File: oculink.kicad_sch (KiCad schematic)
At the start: 17 parts, among them J4 OCuLink_x4_Amphenol_G14A42121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, U10 ESD204DQAR, U11 ESD204DQAR, U8 ESD204DQAR, U9 ESD204DQAR

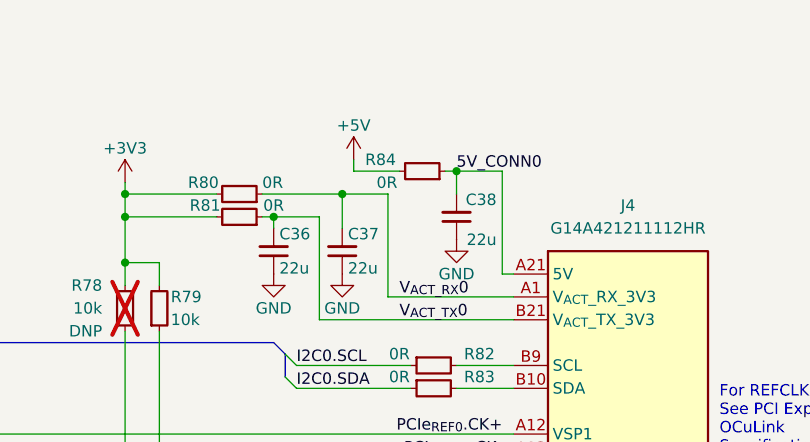
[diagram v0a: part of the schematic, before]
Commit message: [#58137] Add DC/DC supplies
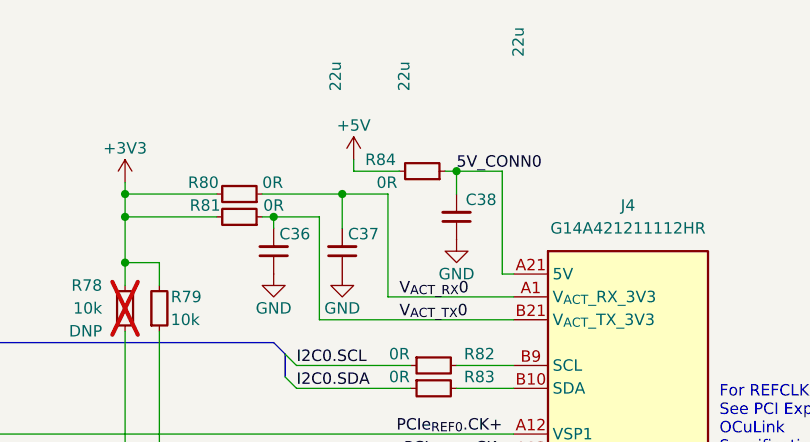
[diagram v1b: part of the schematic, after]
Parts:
- C36, C37, C38: value C_22u_0603 -> C_22u_16V_0603; symbol antmicroCapacitors0603:C_22u_0603 -> antmicroCapacitors0603:C_22u_16V_0603; MPN GRM188R60J226MEA0D -> CL10A226MO7JZNC; Manufacturer Murata -> Samsung Electro-Mechanics; Voltage (none) -> 16V
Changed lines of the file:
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@@
     (effects (font (size 1.27 1.27)) (justify right))
   )
-  (symbol (lib_id "antmicroCapacitors0603:C_22u_0603") (at 231.14 95.25 90) (unit 1)
+  (symbol (lib_id "antmicroCapacitors0603:C_22u_16V_0603") (at 231.14 95.25 90) (unit 1)
     (in_bom yes) (on_board yes) (dnp no)
     (property "Reference" "C38" (at 235.585 90.805 90)
       (effects (font (size 1.27 1.27) (thickness 0.15)) (justify left))
     )
-    (property "Value" "C_22u_0603" (at 241.3 74.93 0)
+    (property "Value" "C_22u_16V_0603" (at 241.3 74.93 0)
       (effects (font (size 1.27 1.27) (thickness 0.15)) (justify left bottom) hide)
     )
@@
       (effects (font (size 1.27 1.27) (thickness 0.15)) (justify left bottom) hide)
     )
-    (property "Datasheet" "https://www.murata.com/products/productdetail?partno=GRM188R60J226MEA0%23" (at 246.38 74.93 0)
-      (effects (font (size 1.27 1.27) (thickness 0.15)) (justify left bottom) hide)
-    )
-    (property "MPN" "GRM188R60J226MEA0D" (at 248.92 74.93 0)
-      (effects (font (size 1.27 1.27) (thickness 0.15)) (justify left bottom) hide)
-    )
-    (property "Manufacturer" "Murata" (at 251.46 74.93 0)
+    (property "Datasheet" "https://product.samsungsem.com/mlcc/CL10A226MO7JZN.do" (at 246.38 74.93 0)
+      (effects (font (size 1.27 1.27) (thickness 0.15)) (justify left bottom) hide)
+    )
+    (property "MPN" "CL10A226MO7JZNC" (at 248.92 74.93 0)
+      (effects (font (size 1.27 1.27) (thickness 0.15)) (justify left bottom) hide)
+    )
+    (property "Manufacturer" "Samsung Electro-Mechanics" (at 251.46 74.93 0)
       (effects (font (size 1.27 1.27) (thickness 0.15)) (justify left bottom) hide)
     )
@@
       (effects (font (size 1.27 1.27) (thickness 0.15)) (justify left bottom) hide)
     )
-    (property "Val" "22u" (at 235.585 95.25 90)
-      (effects (font (size 1.27 1.27) (thickness 0.15)) (justify left))
-    )
-    (property "Voltage" "" (at 259.08 74.93 0)
+    (property "Val" "22u" (at 238.76 74.93 0)
+      (effects (font (size 1.27 1.27) (thickness 0.15)) (justify left bottom))
+    )
+    (property "Voltage" "16V" (at 259.08 74.93 0)
       (effects (font (size 1.27 1.27)) (justify left bottom) hide)
     )
@@
     )
   )
-  (symbol (lib_id "antmicroCapacitors0603:C_22u_0603") (at 210.82 99.06 90) (unit 1)
+  (symbol (lib_id "antmicroCapacitors0603:C_22u_16V_0603") (at 210.82 99.06 90) (unit 1)
     (in_bom yes) (on_board yes) (dnp no)
     (property "Reference" "C36" (at 211.455 94.615 90)
       (effects (font (size 1.27 1.27) (thickness 0.15)) (justify right))
     )
-    (property "Value" "C_22u_0603" (at 220.98 78.74 0)
+    (property "Value" "C_22u_16V_0603" (at 220.98 78.74 0)
       (effects (font (size 1.27 1.27) (thickness 0.15)) (justify left bottom) hide)
     )
@@
       (effects (font (size 1.27 1.27) (thickness 0.15)) (justify left bottom) hide)
     )
-    (property "Datasheet" "https://www.murata.com/products/productdetail?partno=GRM188R60J226MEA0%23" (at 226.06 78.74 0)
-      (effects (font (size 1.27 1.27) (thickness 0.15)) (justify left bottom) hide)
-    )
-    (property "MPN" "GRM188R60J226MEA0D" (at 228.6 78.74 0)
-      (effects (font (size 1.27 1.27) (thickness 0.15)) (justify left bottom) hide)
-    )
-    (property "Manufacturer" "Murata" (at 231.14 78.74 0)
+    (property "Datasheet" "https://product.samsungsem.com/mlcc/CL10A226MO7JZN.do" (at 226.06 78.74 0)
+      (effects (font (size 1.27 1.27) (thickness 0.15)) (justify left bottom) hide)
+    )
+    (property "MPN" "CL10A226MO7JZNC" (at 228.6 78.74 0)
+      (effects (font (size 1.27 1.27) (thickness 0.15)) (justify left bottom) hide)
+    )
+    (property "Manufacturer" "Samsung Electro-Mechanics" (at 231.14 78.74 0)
       (effects (font (size 1.27 1.27) (thickness 0.15)) (justify left bottom) hide)
     )
@@
       (effects (font (size 1.27 1.27) (thickness 0.15)) (justify left bottom) hide)
     )
-    (property "Val" "22u" (at 211.455 98.425 90)
-      (effects (font (size 1.27 1.27) (thickness 0.15)) (justify right))
-    )
-    (property "Voltage" "" (at 238.76 78.74 0)
+    (property "Val" "22u" (at 218.44 78.74 0)
+      (effects (font (size 1.27 1.27) (thickness 0.15)) (justify left bottom))
+    )
+    (property "Voltage" "16V" (at 238.76 78.74 0)
       (effects (font (size 1.27 1.27)) (justify left bottom) hide)
     )
@@
     )
   )
-  (symbol (lib_id "antmicroCapacitors0603:C_22u_0603") (at 218.44 99.06 90) (unit 1)
+  (symbol (lib_id "antmicroCapacitors0603:C_22u_16V_0603") (at 218.44 99.06 90) (unit 1)
     (in_bom yes) (on_board yes) (dnp no)
     (property "Reference" "C37" (at 219.075 94.615 90)
       (effects (font (size 1.27 1.27) (thickness 0.15)) (justify right))
     )
-    (property "Value" "C_22u_0603" (at 228.6 78.74 0)
+    (property "Value" "C_22u_16V_0603" (at 228.6 78.74 0)
       (effects (font (size 1.27 1.27) (thickness 0.15)) (justify left bottom) hide)
     )
@@
       (effects (font (size 1.27 1.27) (thickness 0.15)) (justify left bottom) hide)
     )
-    (property "Datasheet" "https://www.murata.com/products/productdetail?partno=GRM188R60J226MEA0%23" (at 233.68 78.74 0)
-      (effects (font (size 1.27 1.27) (thickness 0.15)) (justify left bottom) hide)
-    )
-    (property "MPN" "GRM188R60J226MEA0D" (at 236.22 78.74 0)
-      (effects (font (size 1.27 1.27) (thickness 0.15)) (justify left bottom) hide)
-    )
-    (property "Manufacturer" "Murata" (at 238.76 78.74 0)
+    (property "Datasheet" "https://product.samsungsem.com/mlcc/CL10A226MO7JZN.do" (at 233.68 78.74 0)
+      (effects (font (size 1.27 1.27) (thickness 0.15)) (justify left bottom) hide)
+    )
+    (property "MPN" "CL10A226MO7JZNC" (at 236.22 78.74 0)
+      (effects (font (size 1.27 1.27) (thickness 0.15)) (justify left bottom) hide)
+    )
+    (property "Manufacturer" "Samsung Electro-Mechanics" (at 238.76 78.74 0)
       (effects (font (size 1.27 1.27) (thickness 0.15)) (justify left bottom) hide)
     )
@@
       (effects (font (size 1.27 1.27) (thickness 0.15)) (justify left bottom) hide)
     )
-    (property "Val" "22u" (at 219.075 98.425 90)
-      (effects (font (size 1.27 1.27) (thickness 0.15)) (justify right))
-    )
-    (property "Voltage" "" (at 246.38 78.74 0)
-      (effects (font (size 1.27 1.27)) (justify left bottom) hide)
-    )
+    (property "Val" "22u" (at 226.06 78.74 0)
+      (effects (font (size 1.27 1.27) (thickness 0.15)) (justify left bottom))
+    )
+    (property "Voltage" "16V" (at 246.38 78.74 0)
+      (effects (font (size 1.27 1.27)) (justify left bottom) hide)
+    )

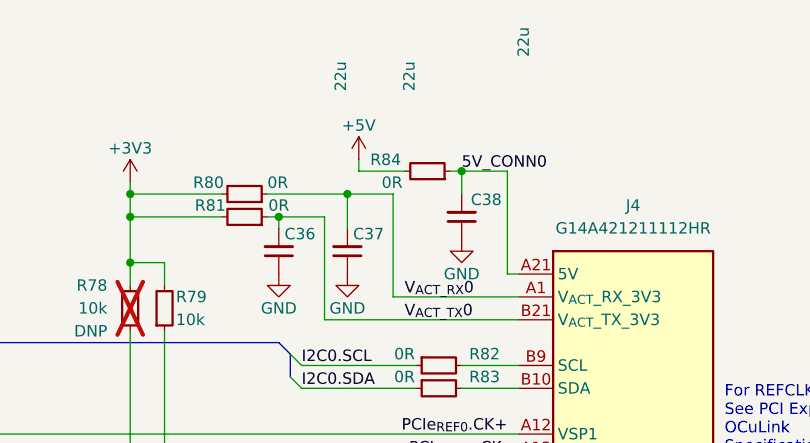
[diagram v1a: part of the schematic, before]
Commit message: [#58137] Add power sequencing and reset
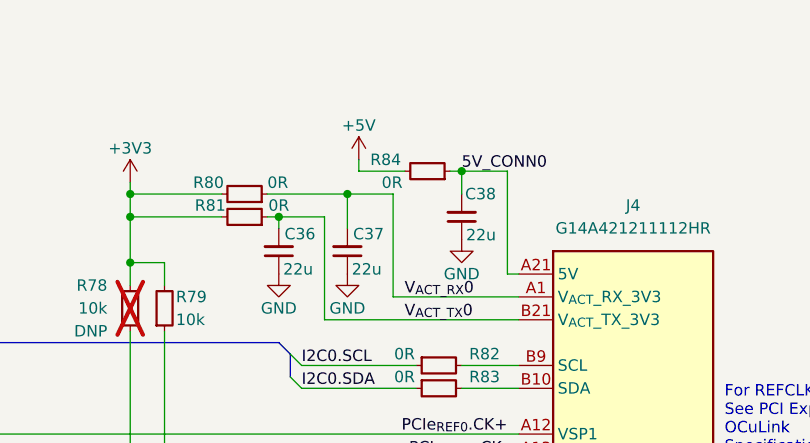
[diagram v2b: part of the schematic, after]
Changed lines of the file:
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@@
   (symbol (lib_id "antmicroCapacitors0603:C_22u_16V_0603") (at 231.14 95.25 90) (unit 1)
     (in_bom yes) (on_board yes) (dnp no)
-    (property "Reference" "C38" (at 235.585 90.805 90)
+    (property "Reference" "C38" (at 234.95 90.17 90)
       (effects (font (size 1.27 1.27) (thickness 0.15)) (justify left))
     )
@@
       (effects (font (size 1.27 1.27) (thickness 0.15)) (justify left bottom) hide)
     )
-    (property "Val" "22u" (at 238.76 74.93 0)
+    (property "Val" "22u" (at 234.95 93.98 90)
       (effects (font (size 1.27 1.27) (thickness 0.15)) (justify left bottom))
     )
@@
       (effects (font (size 1.27 1.27) (thickness 0.15)) (justify left bottom) hide)
     )
-    (property "Val" "22u" (at 218.44 78.74 0)
+    (property "Val" "22u" (at 214.63 97.79 90)
       (effects (font (size 1.27 1.27) (thickness 0.15)) (justify left bottom))
     )
@@
       (effects (font (size 1.27 1.27) (thickness 0.15)) (justify left bottom) hide)
     )
-    (property "Val" "22u" (at 226.06 78.74 0)
+    (property "Val" "22u" (at 222.25 97.79 90)
       (effects (font (size 1.27 1.27) (thickness 0.15)) (justify left bottom))
     )

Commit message: Fix ERC
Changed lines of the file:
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@@
   (junction (at 194.31 124.46) (diameter 0) (color 0 0 0 0)
   )
+  (junction (at 223.52 95.25) (diameter 0) (color 0 0 0 0)
+  )
   (junction (at 264.16 190.5) (diameter 0) (color 0 0 0 0)
   )
@@
   )
   (junction (at 231.14 87.63) (diameter 0) (color 0 0 0 0)
+  )
+  (junction (at 215.9 104.14) (diameter 0) (color 0 0 0 0)
   )
   (junction (at 194.31 97.79) (diameter 0) (color 0 0 0 0)
@@
     (stroke (width 0) (type default))
   )
-  (wire (pts (xy 223.52 101.6) (xy 223.52 90.17))
+  (wire (pts (xy 223.52 101.6) (xy 223.52 95.25))
     (stroke (width 0) (type default))
   )
@@
   )
   (wire (pts (xy 209.55 92.71) (xy 210.82 92.71))
+    (stroke (width 0) (type default))
+  )
+  (wire (pts (xy 223.52 95.25) (xy 223.52 90.17))
     (stroke (width 0) (type default))
   )
@@
     )
   )
+  (symbol (lib_id "antmicropower:PWR_FLAG") (at 223.52 95.25 270) (unit 1)
+    (in_bom yes) (on_board yes) (dnp no) (fields_autoplaced)
+    (property "Reference" "#FLG010" (at 225.425 95.25 0)
+      (effects (font (size 1.27 1.27)) hide)
+    )
+    (property "Value" "PWR_FLAG" (at 227.33 95.2499 90)
+      (effects (font (size 1.27 1.27)) (justify left) hide)
+    )
+    (property "Footprint" "" (at 223.52 95.25 0)
+      (effects (font (size 1.27 1.27)) hide)
+    )
+    (property "Datasheet" "" (at 223.52 95.25 0)
+      (effects (font (size 1.27 1.27)) hide)
+    )
+    (pin "1")
+    (instances
+      (project "com-express-7-baseboard"
+        (path "/1b8c34da-dad5-4b0b-8c4b-45db766c4dfa/b09f3a23-0194-4388-b358-3a9807b09321"
+          (reference "#FLG010") (unit 1)
+        )
+      )
+    )
+  )
   (symbol (lib_id "antmicroTVSDiodes:ESD204DQAR") (at 287.02 134.62 0) (unit 1)
     (in_bom yes) (on_board yes) (dnp no) (fields_autoplaced)
@@
         )
       )
+    )
+  )
+  (symbol (lib_id "antmicropower:PWR_FLAG") (at 215.9 104.14 90) (unit 1)
+    (in_bom yes) (on_board yes) (dnp no) (fields_autoplaced)
+    (property "Reference" "#FLG011" (at 213.995 104.14 0)
+      (effects (font (size 1.27 1.27)) hide)
+    )
+    (property "Value" "PWR_FLAG" (at 212.09 104.1399 90)
+      (effects (font (size 1.27 1.27)) (justify left) hide)
+    )
+    (property "Footprint" "" (at 215.9 104.14 0)
+      (effects (font (size 1.27 1.27)) hide)
+    )
+    (property "Datasheet" "" (at 215.9 104.14 0)
+      (effects (font (size 1.27 1.27)) hide)
+    )
+    (pin "1")
+    (instances
+      (project "com-express-7-baseboard"
+        (path "/1b8c34da-dad5-4b0b-8c4b-45db766c4dfa/b09f3a23-0194-4388-b358-3a9807b09321"
+          (reference "#FLG011") (unit 1)
+        )
+      )

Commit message: Optimize BOM, reannotate
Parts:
- removed R84: R_0R_0603, antmicro-footprints:R_0603_1608Metric, symbol antmicroResistors0603:R_0R_0603
- added R82: R_0R001_0805, antmicro-footprints:R_0805_2012Metric, symbol antmicroResistorsmisc:R_0R001_0805
- renumbered R82 to R83, R83 to R84
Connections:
- net +5V: now also R82.1
- net 5V_CONN0: now also R82.2
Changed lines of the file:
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@@
+    )
+  )
+  (symbol (lib_id "antmicroResistorsmisc:R_0R001_0805") (at 224.79 87.63 0) (unit 1)
+    (in_bom yes) (on_board yes) (dnp no)
+    (property "Reference" "R82" (at 227.33 82.55 0)
+      (effects (font (size 1.27 1.27) (thickness 0.15)))
+    )
+    (property "Value" "R_0R001_0805" (at 245.11 100.33 0)
+      (effects (font (size 1.27 1.27) (thickness 0.15)) (justify left bottom) hide)
+    )
+    (property "Footprint" "antmicro-footprints:R_0805_2012Metric" (at 245.11 102.87 0)
+      (effects (font (size 1.27 1.27) (thickness 0.15)) (justify left bottom) hide)
+    )
+    (property "Datasheet" "https://www.bourns.com/docs/product-datasheets/cr.pdf" (at 245.11 105.41 0)
+      (effects (font (size 1.27 1.27) (thickness 0.15)) (justify left bottom) hide)
+    )
+    (property "MPN" "MSMA0805R0010FSM" (at 245.11 107.95 0)
+      (effects (font (size 1.27 1.27) (thickness 0.15)) (justify left bottom) hide)
+    )
+    (property "Manufacturer" "Eaton" (at 245.11 110.49 0)
+      (effects (font (size 1.27 1.27) (thickness 0.15)) (justify left bottom) hide)
+    )
+    (property "License" "Apache-2.0" (at 245.11 113.03 0)
+      (effects (font (size 1.27 1.27) (thickness 0.15)) (justify left bottom) hide)
+    )
+    (property "Author" "Antmicro" (at 245.11 115.57 0)
+      (effects (font (size 1.27 1.27) (thickness 0.15)) (justify left bottom) hide)
+    )
+    (property "Val" "0R001" (at 227.33 85.09 0)
+      (effects (font (size 1.27 1.27) (thickness 0.15)))
+    )
+    (property "Tolerance" "1%" (at 245.11 97.79 0)
+      (effects (font (size 1.27 1.27)) (justify left bottom) hide)
+    )
+    (pin "2")
+    (pin "1")
+    (instances
+      (project "com-express-7-baseboard"
+        (path "/1b8c34da-dad5-4b0b-8c4b-45db766c4dfa/b09f3a23-0194-4388-b358-3a9807b09321"
+          (reference "R82") (unit 1)
+        )
+      )
     )
   )
@@
     )
   )
-  (symbol (lib_id "antmicroResistors0603:R_0R_0603") (at 229.87 87.63 180) (unit 1)
-    (in_bom yes) (on_board yes) (dnp no)
-    (property "Reference" "R84" (at 220.98 86.36 0)
-      (effects (font (size 1.27 1.27) (thickness 0.15)) (justify right))
-    )
-    (property "Value" "R_0R_0603" (at 209.55 74.93 0)
-      (effects (font (size 1.27 1.27) (thickness 0.15)) (justify left bottom) hide)
-    )
-    (property "Footprint" "antmicro-footprints:R_0603_1608Metric" (at 209.55 72.39 0)
-      (effects (font (size 1.27 1.27) (thickness 0.15)) (justify left bottom) hide)
-    )
-    (property "Datasheet" "https://www.bourns.com/docs/product-datasheets/cr.pdf?sfvrsn=574d41f6_14" (at 209.55 69.85 0)
-      (effects (font (size 1.27 1.27) (thickness 0.15)) (justify left bottom) hide)
-    )
-    (property "MPN" "CR0603-J/-000ELF" (at 209.55 67.31 0)
-      (effects (font (size 1.27 1.27) (thickness 0.15)) (justify left bottom) hide)
-    )
-    (property "Manufacturer" "Bourns" (at 209.55 64.77 0)
-      (effects (font (size 1.27 1.27) (thickness 0.15)) (justify left bottom) hide)
-    )
-    (property "License" "Apache-2.0" (at 209.55 62.23 0)
-      (effects (font (size 1.27 1.27) (thickness 0.15)) (justify left bottom) hide)
-    )
-    (property "Author" "Antmicro" (at 209.55 59.69 0)
-      (effects (font (size 1.27 1.27) (thickness 0.15)) (justify left bottom) hide)
-    )
-    (property "Val" "0R" (at 222.25 88.9 0)
-      (effects (font (size 1.27 1.27) (thickness 0.15)) (justify right))
-    )
-    (property "Tolerance" "~" (at 209.55 77.47 0)
-      (effects (font (size 1.27 1.27)) (justify left bottom) hide)
-    )
-    (property "Current" "1A" (at 209.55 57.15 0)
-      (effects (font (size 1.27 1.27) (thickness 0.15)) (justify left bottom) hide)
-    )
-    (pin "2")
-    (pin "1")
-    (instances
-      (project "com-express-7-baseboard"
-        (path "/1b8c34da-dad5-4b0b-8c4b-45db766c4dfa/b09f3a23-0194-4388-b358-3a9807b09321"
-          (reference "R84") (unit 1)
-        )
-      )
-    )
-  )
   (symbol (lib_id "antmicropower:+3V3") (at 194.31 88.9 0) (unit 1)
     (in_bom yes) (on_board yes) (dnp no)
@@
   (symbol (lib_id "antmicroResistors0402:R_0R_0402") (at 226.06 109.22 0) (unit 1)
     (in_bom yes) (on_board yes) (dnp no)
-    (property "Reference" "R82" (at 233.68 107.95 0)
+    (property "Reference" "R83" (at 233.68 107.95 0)
       (effects (font (size 1.27 1.27) (thickness 0.15)))
     )
@@
       (project "com-express-7-baseboard"
         (path "/1b8c34da-dad5-4b0b-8c4b-45db766c4dfa/b09f3a23-0194-4388-b358-3a9807b09321"
-          (reference "R82") (unit 1)
+          (reference "R83") (unit 1)
         )
       )
@@
   (symbol (lib_id "antmicroResistors0402:R_0R_0402") (at 226.06 111.76 0) (unit 1)
     (in_bom yes) (on_board yes) (dnp no)
-    (property "Reference" "R83" (at 233.68 110.49 0)
+    (property "Reference" "R84" (at 233.68 110.49 0)
       (effects (font (size 1.27 1.27) (thickness 0.15)))
     )
@@
       (project "com-express-7-baseboard"
         (path "/1b8c34da-dad5-4b0b-8c4b-45db766c4dfa/b09f3a23-0194-4388-b358-3a9807b09321"
-          (reference "R83") (unit 1)
-        )
-      )
+          (reference "R84") (unit 1)
+        )
+      )

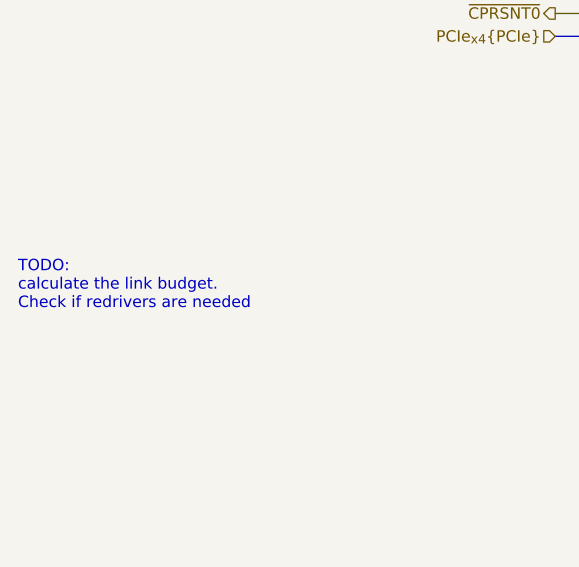
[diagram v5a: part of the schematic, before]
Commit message: [#58137] Add power monitors; clean up I2C bus
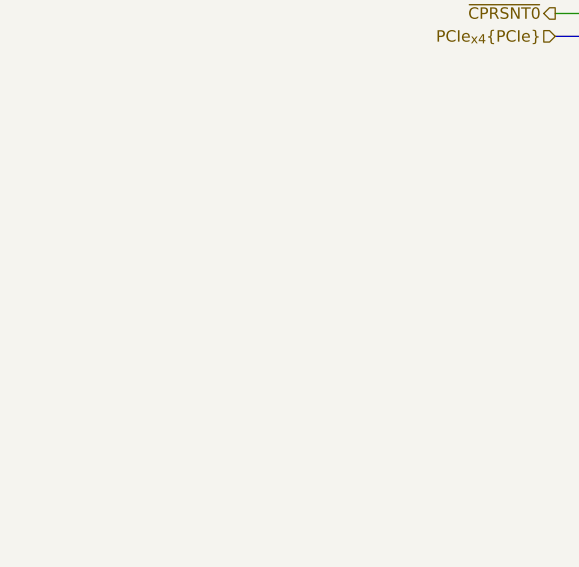
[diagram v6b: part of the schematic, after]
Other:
- note removed: "TODO: calculate the link budget. Check if redrivers are needed"
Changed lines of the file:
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@@
     (stroke (width 0) (type default))
-  )
-  (text "TODO: \ncalculate the link budget.\nCheck if redrivers are needed"
-    (at 111.76 160.02 0)
-    (effects (font (size 1.27 1.27)) (justify left bottom))
   )
   (text "For REFCLK\nSee PCI Express\nOCuLink\nSpecification\nRevision 1.0\nTable 2-2 note 2"
